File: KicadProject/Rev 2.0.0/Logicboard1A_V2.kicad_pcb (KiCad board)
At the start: 6 copper layers, 45 x 45 mm, 181 parts, among them J601 2337019-1, J602 2337019-1, U101 STM32MP15xxAC3, U201 AS4C256M16D3LC-12BCN, U401 STPMIC1xPQR, U501 S40FC004C1B2C00000, U601 LBEE59B1LV-278, U701 DF40C-70DP-0.4V(51), U702 DF40C-70DP-0.4V(51), U703 DF40C-70DP-0.4V(51), X101 32.768kHz, Y101 24MHz

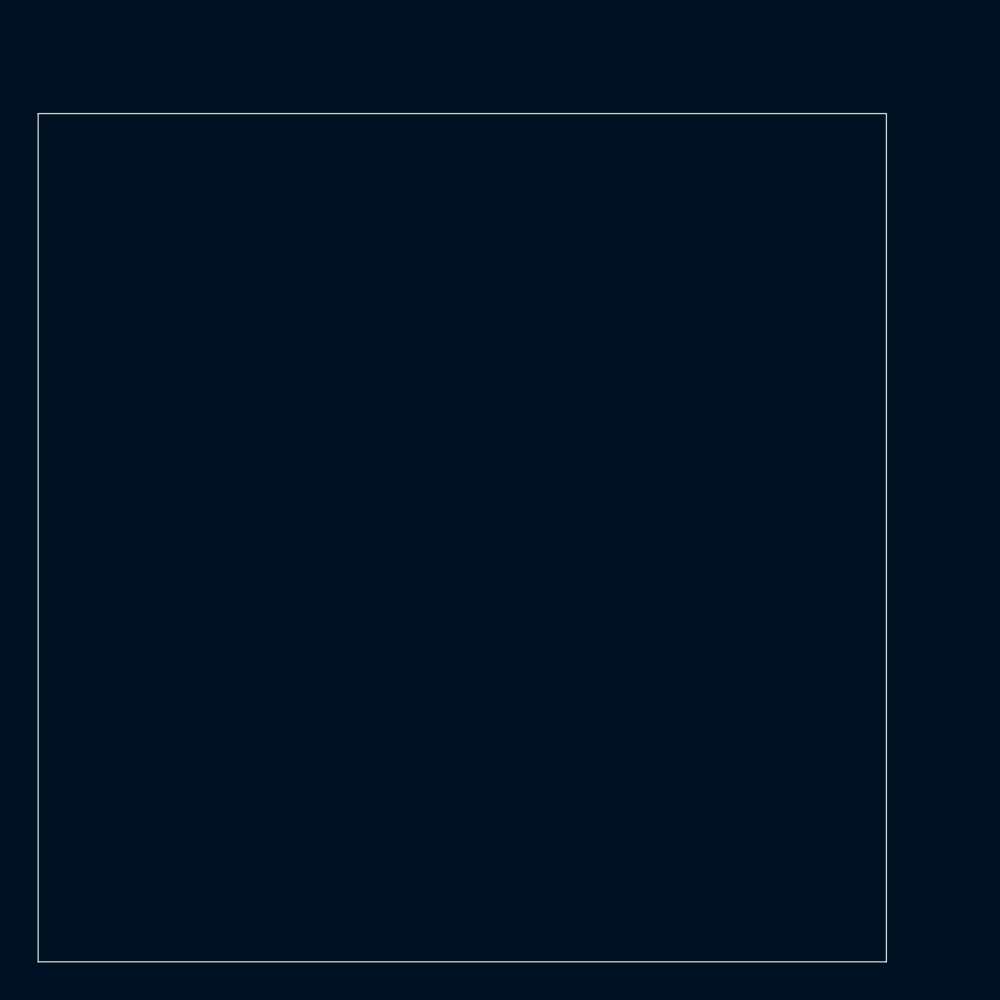
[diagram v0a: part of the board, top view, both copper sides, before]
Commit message: BT_RF_IN pin connected to ground
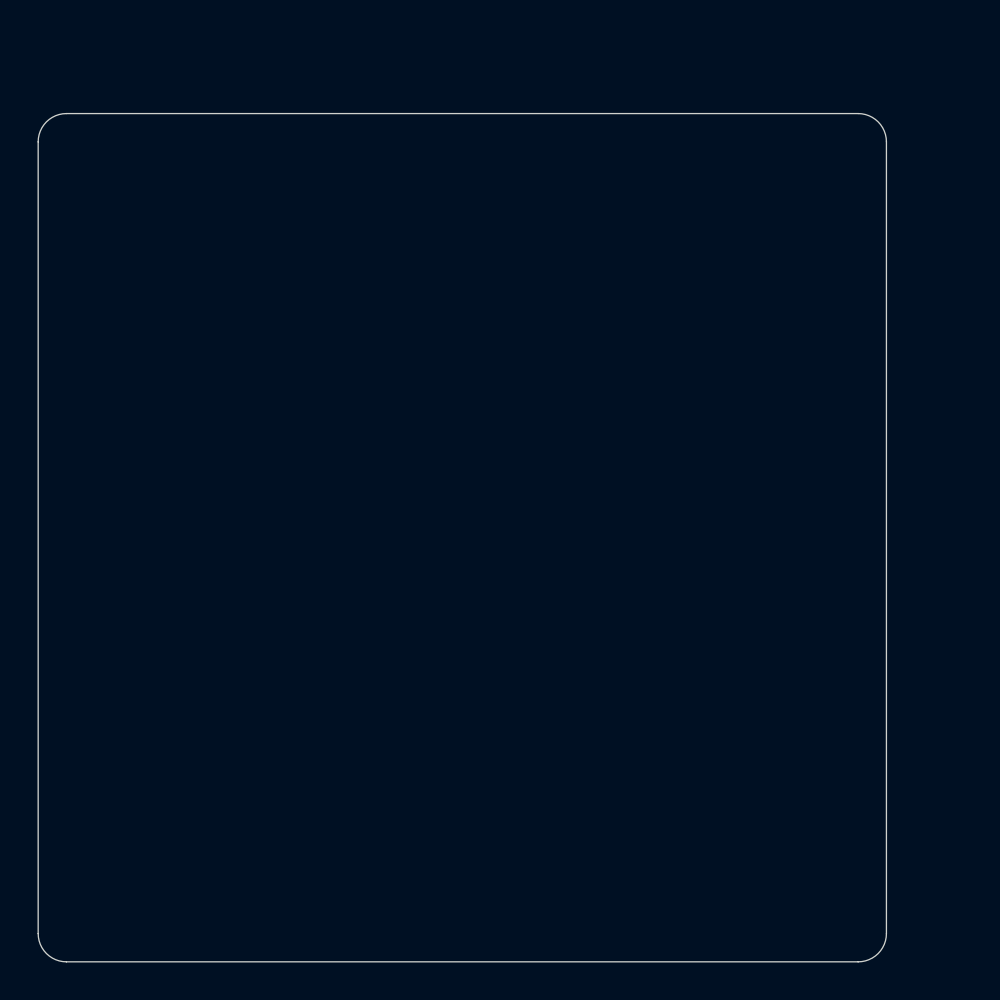
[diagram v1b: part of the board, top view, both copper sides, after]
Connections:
- net BT_RF_IN renamed GND
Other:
- outline, holes or cut-outs redrawn
- net class Default: clearance 0.2 -> 0.08; trace_width 0.25 -> 0.09; via_dia 0.8 -> 0.4; via_drill 0.4 -> 0.2
- rule trace_clearance: 0.2 -> 0.08
- rule trace_min: 0.2 -> 0.09
- rule via_min_drill: 0.3 -> 0.2

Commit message: just before starting placement
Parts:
- FID701, FID704: moved to B.Cu
- moved FID704 214.2 mm to (141.7, 123.2)
- moved FID702 211.4 mm to (141.7, 123.2)
- moved FID701 201.8 mm to (141.7, 86.1)
- moved FID706 198.9 mm to (141.7, 86.1)
- moved H702 192.8 mm to (142.3, 82.3)
- moved FID705 170.2 mm to (179.0, 123.2)
- moved H701 169.9 mm to (182.7, 122.7)
- moved FID703 168.7 mm to (179.0, 123.2)
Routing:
- added copper zone on L4_Gnd_Signal.Cu, net (none)
- added copper zone on L5_Gnd.Cu, net (none)
- added copper zone on L2_Gnd.Cu, net GND
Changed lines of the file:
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@@
     (4 L5_Gnd.Cu power)
     (31 L6_Sig_Pwr.Cu mixed)
-    (32 B.Adhes user)
-    (33 F.Adhes user)
-    (34 B.Paste user)
-    (35 F.Paste user)
-    (36 B.SilkS user)
-    (37 F.SilkS user)
-    (38 B.Mask user)
-    (39 F.Mask user)
-    (40 Dwgs.User user)
-    (41 Cmts.User user)
-    (42 Eco1.User user)
-    (43 Eco2.User user)
+    (32 B.Adhes user hide)
+    (33 F.Adhes user hide)
+    (34 B.Paste user hide)
+    (35 F.Paste user hide)
+    (36 B.SilkS user hide)
+    (37 F.SilkS user hide)
+    (38 B.Mask user hide)
+    (39 F.Mask user hide)
+    (40 Dwgs.User user hide)
+    (41 Cmts.User user hide)
+    (42 Eco1.User user hide)
+    (43 Eco2.User user hide)
     (44 Edge.Cuts user)
-    (45 Margin user)
+    (45 Margin user hide)
     (46 B.CrtYd user)
     (47 F.CrtYd user)
-    (48 B.Fab user)
-    (49 F.Fab user)
+    (48 B.Fab user hide)
+    (49 F.Fab user hide)
   )
   (setup
@@
     (user_trace_width 0.7)
     (trace_clearance 0.08)
-    (zone_clearance 0.508)
+    (zone_clearance 0.1)
     (zone_45_only no)
     (trace_min 0.09)
@@
   )
   (module U_MountingHole:MountingHole_2.2mm_M2_DIN965_Pad (layer L1_Sig_Pwr.Cu)
-    (at 327.48 28.51)
+    (at 142.3 82.3)
     (descr "Mounting Hole 2.2mm, M2, DIN965")
     (tags "mounting hole 2.2mm m2 din965")
@@
   )
   (module U_MountingHole:MountingHole_2.2mm_M2_DIN965_Pad (layer L1_Sig_Pwr.Cu)
-    (at 327.48 33.86)
+    (at 182.7 122.7)
     (descr "Mounting Hole 2.2mm, M2, DIN965")
     (tags "mounting hole 2.2mm m2 din965")
@@
   )
   (module U_Fiducial:Fiducial_0.5mm_Mask1.5mm (layer L1_Sig_Pwr.Cu)
-    (at 331.68 27.36)
+    (at 141.7 86.1)
     (descr "Circular Fiducial, 0.5mm bare copper, 1.5mm soldermask opening")
     (tags fiducial)
@@
   )
   (module U_Fiducial:Fiducial_0.5mm_Mask1.5mm (layer L1_Sig_Pwr.Cu)
-    (at 326.33 38.06)
+    (at 179 123.2)
     (descr "Circular Fiducial, 0.5mm bare copper, 1.5mm soldermask opening")
     (tags fiducial)
@@
       (solder_mask_margin 0.5) (clearance 0.5))
   )
-  (module U_Fiducial:Fiducial_0.5mm_Mask1.5mm (layer L1_Sig_Pwr.Cu)
-    (at 334.73 30.41)
+  (module U_Fiducial:Fiducial_0.5mm_Mask1.5mm (layer L6_Sig_Pwr.Cu)
+    (at 141.7 123.2)
     (descr "Circular Fiducial, 0.5mm bare copper, 1.5mm soldermask opening")
     (tags fiducial)
     (attr smd)
-    (fp_text reference FID704 (at 0 -1.7145) (layer F.SilkS) hide
-      (effects (font (size 1 1) (thickness 0.15)))
+    (fp_text reference FID704 (at 0 1.7145) (layer B.SilkS) hide
+      (effects (font (size 1 1) (thickness 0.15)) (justify mirror))
     )
-    (fp_text value Fiducial (at 0 1.7145) (layer F.Fab) hide
-      (effects (font (size 1 1) (thickness 0.15)))
+    (fp_text value Fiducial (at 0 -1.7145) (layer B.Fab) hide
+      (effects (font (size 1 1) (thickness 0.15)) (justify mirror))
     )
-    (fp_circle (center 0 0) (end 0.75 0) (layer F.Fab) (width 0.1))
-    (fp_circle (center 0 0) (end 1 0) (layer F.CrtYd) (width 0.05))
-    (fp_text user %R (at 0 0) (layer F.Fab)
-      (effects (font (size 0.2 0.2) (thickness 0.04)))
+    (fp_circle (center 0 0) (end 0.75 0) (layer B.Fab) (width 0.1))
+    (fp_circle (center 0 0) (end 1 0) (layer B.CrtYd) (width 0.05))
+    (fp_text user %R (at 0 0) (layer B.Fab)
+      (effects (font (size 0.2 0.2) (thickness 0.04)) (justify mirror))
     )
-    (pad "" smd circle (at 0 0) (size 0.5 0.5) (layers L1_Sig_Pwr.Cu F.Mask)
+    (pad "" smd circle (at 0 0) (size 0.5 0.5) (layers L6_Sig_Pwr.Cu B.Mask)
       (solder_mask_margin 0.5) (clearance 0.5))
   )
   (module U_Fiducial:Fiducial_0.5mm_Mask1.5mm (layer L1_Sig_Pwr.Cu)
-    (at 326.33 41.11)
+    (at 179 123.2)
     (descr "Circular Fiducial, 0.5mm bare copper, 1.5mm soldermask opening")
     (tags fiducial)
@@
   )
   (module U_Fiducial:Fiducial_0.5mm_Mask1.5mm (layer L1_Sig_Pwr.Cu)
-    (at 331.68 30.41)
+    (at 141.7 123.2)
     (descr "Circular Fiducial, 0.5mm bare copper, 1.5mm soldermask opening")
     (tags fiducial)
@@
       (solder_mask_margin 0.5) (clearance 0.5))
   )
-  (module U_Fiducial:Fiducial_0.5mm_Mask1.5mm (layer L1_Sig_Pwr.Cu)
-    (at 334.73 27.36)
+  (module U_Fiducial:Fiducial_0.5mm_Mask1.5mm (layer L6_Sig_Pwr.Cu)
+    (at 141.7 86.1)
     (descr "Circular Fiducial, 0.5mm bare copper, 1.5mm soldermask opening")
     (tags fiducial)
     (attr smd)
-    (fp_text reference FID701 (at 0 -1.7145) (layer F.SilkS) hide
-      (effects (font (size 1 1) (thickness 0.15)))
+    (fp_text reference FID701 (at 0 1.7145) (layer B.SilkS) hide
+      (effects (font (size 1 1) (thickness 0.15)) (justify mirror))
     )
-    (fp_text value Fiducial (at 0 1.7145) (layer F.Fab) hide
-      (effects (font (size 1 1) (thickness 0.15)))
+    (fp_text value Fiducial (at 0 -1.7145) (layer B.Fab) hide
+      (effects (font (size 1 1) (thickness 0.15)) (justify mirror))
     )
-    (fp_circle (center 0 0) (end 0.75 0) (layer F.Fab) (width 0.1))
-    (fp_circle (center 0 0) (end 1 0) (layer F.CrtYd) (width 0.05))
-    (fp_text user %R (at 0 0) (layer F.Fab)
-      (effects (font (size 0.2 0.2) (thickness 0.04)))
+    (fp_circle (center 0 0) (end 0.75 0) (layer B.Fab) (width 0.1))
+    (fp_circle (center 0 0) (end 1 0) (layer B.CrtYd) (width 0.05))
+    (fp_text user %R (at 0 0) (layer B.Fab)
+      (effects (font (size 0.2 0.2) (thickness 0.04)) (justify mirror))
     )
-    (pad "" smd circle (at 0 0) (size 0.5 0.5) (layers L1_Sig_Pwr.Cu F.Mask)
+    (pad "" smd circle (at 0 0) (size 0.5 0.5) (layers L6_Sig_Pwr.Cu B.Mask)
       (solder_mask_margin 0.5) (clearance 0.5))
   )
@@
   (gr_line (start 185 81.5) (end 185 123.5) (layer Edge.Cuts) (width 0.05))
   (gr_line (start 141.5 80) (end 183.5 80) (layer Edge.Cuts) (width 0.05))
+  (zone (net 497) (net_name GND) (layer L2_Gnd.Cu) (hatch edge 0.508)
+    (connect_pads yes (clearance 0.1))
+    (min_thickness 0.1)
+    (fill yes (arc_segments 32) (thermal_gap 0.508) (thermal_bridge_width 0.508))
+    (polygon
+      (pts
+        (xy 185 125) (xy 140 125) (xy 140 80) (xy 185 80)
+      )
+    )
+  )
+  (zone (net 0) (net_name "") (layer L4_Gnd_Signal.Cu) (hatch edge 0.508)
+    (connect_pads yes (clearance 0.1))
+    (min_thickness 0.1)
+    (fill yes (arc_segments 32) (thermal_gap 0.508) (thermal_bridge_width 0.508))
+    (polygon
+      (pts
+        (xy 185 125) (xy 140 125) (xy 140 80) (xy 185 80)
+      )
+    )
+  )
+  (zone (net 0) (net_name "") (layer L5_Gnd.Cu) (hatch edge 0.508)
+    (connect_pads yes (clearance 0.1))
+    (min_thickness 0.1)
+    (fill yes (arc_segments 32) (thermal_gap 0.508) (thermal_bridge_width 0.508))
+    (polygon
+      (pts
+        (xy 185 125) (xy 140 125) (xy 140 80) (xy 185 80)
+      )
+    )
+  )
 )

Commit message: V3 initial commit
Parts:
- moved U101 227.6 mm to (169.0, 115.0), turned to 90 degrees
- moved U401 206.2 mm to (153.5, 98.5), turned to 270 degrees
- moved U501 201.5 mm to (151.7, 115.3), turned to 270 degrees
- moved U601 188.8 mm to (162.9, 85.6), turned to 180 degrees
- moved U201 148.5 mm to (168.8, 98.3)
